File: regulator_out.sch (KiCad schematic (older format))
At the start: 36 parts

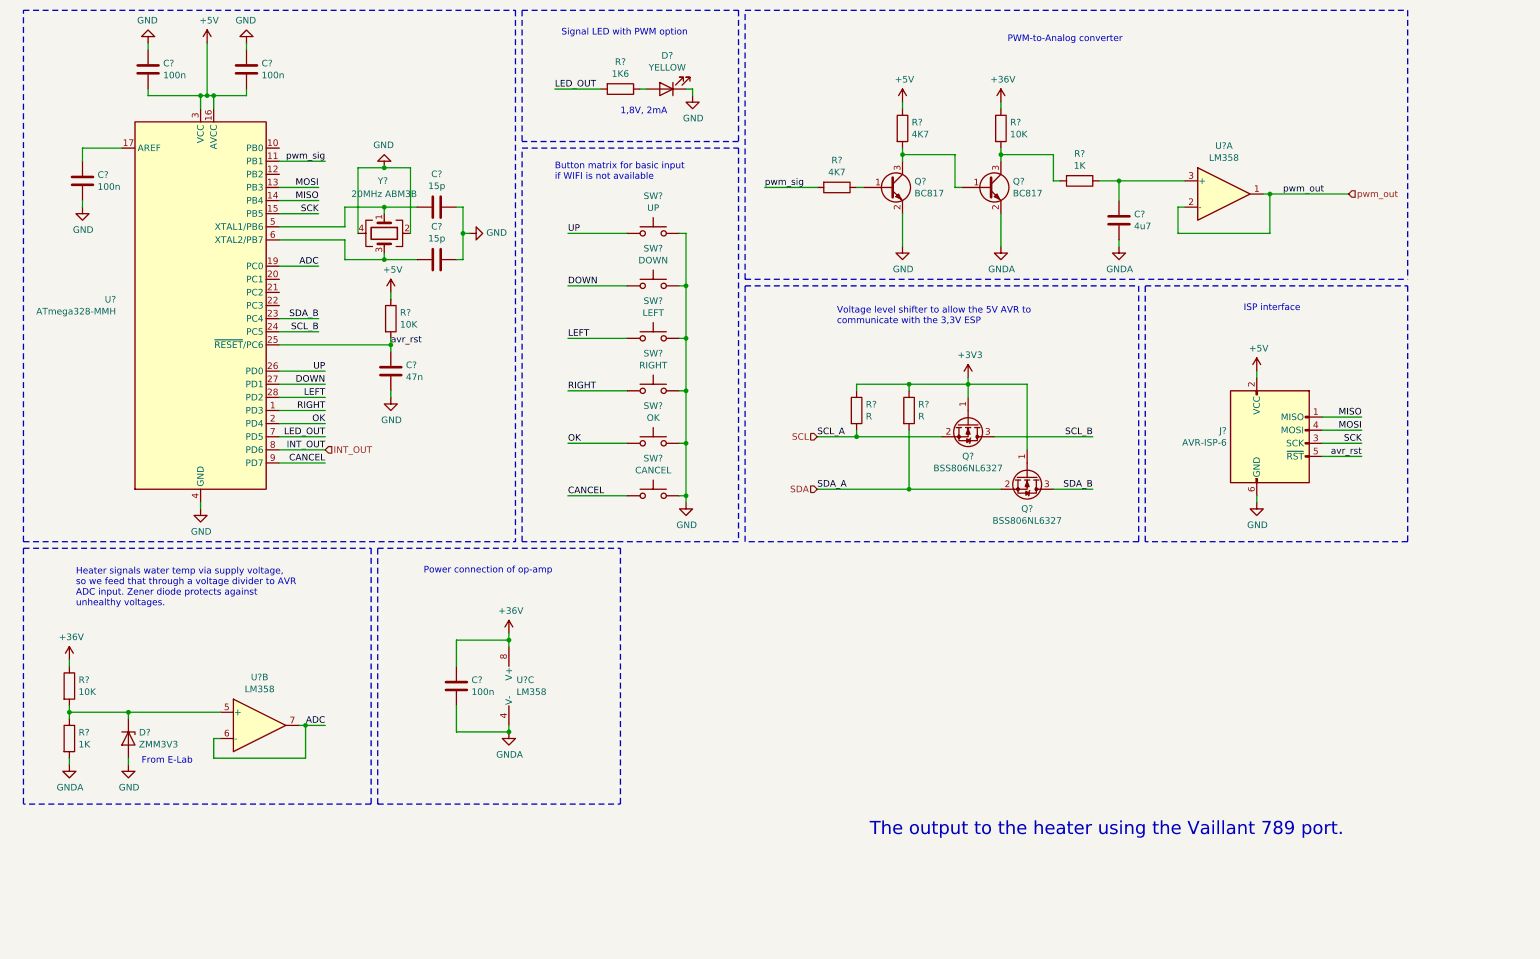
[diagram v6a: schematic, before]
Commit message: Added footprints to most symbols.
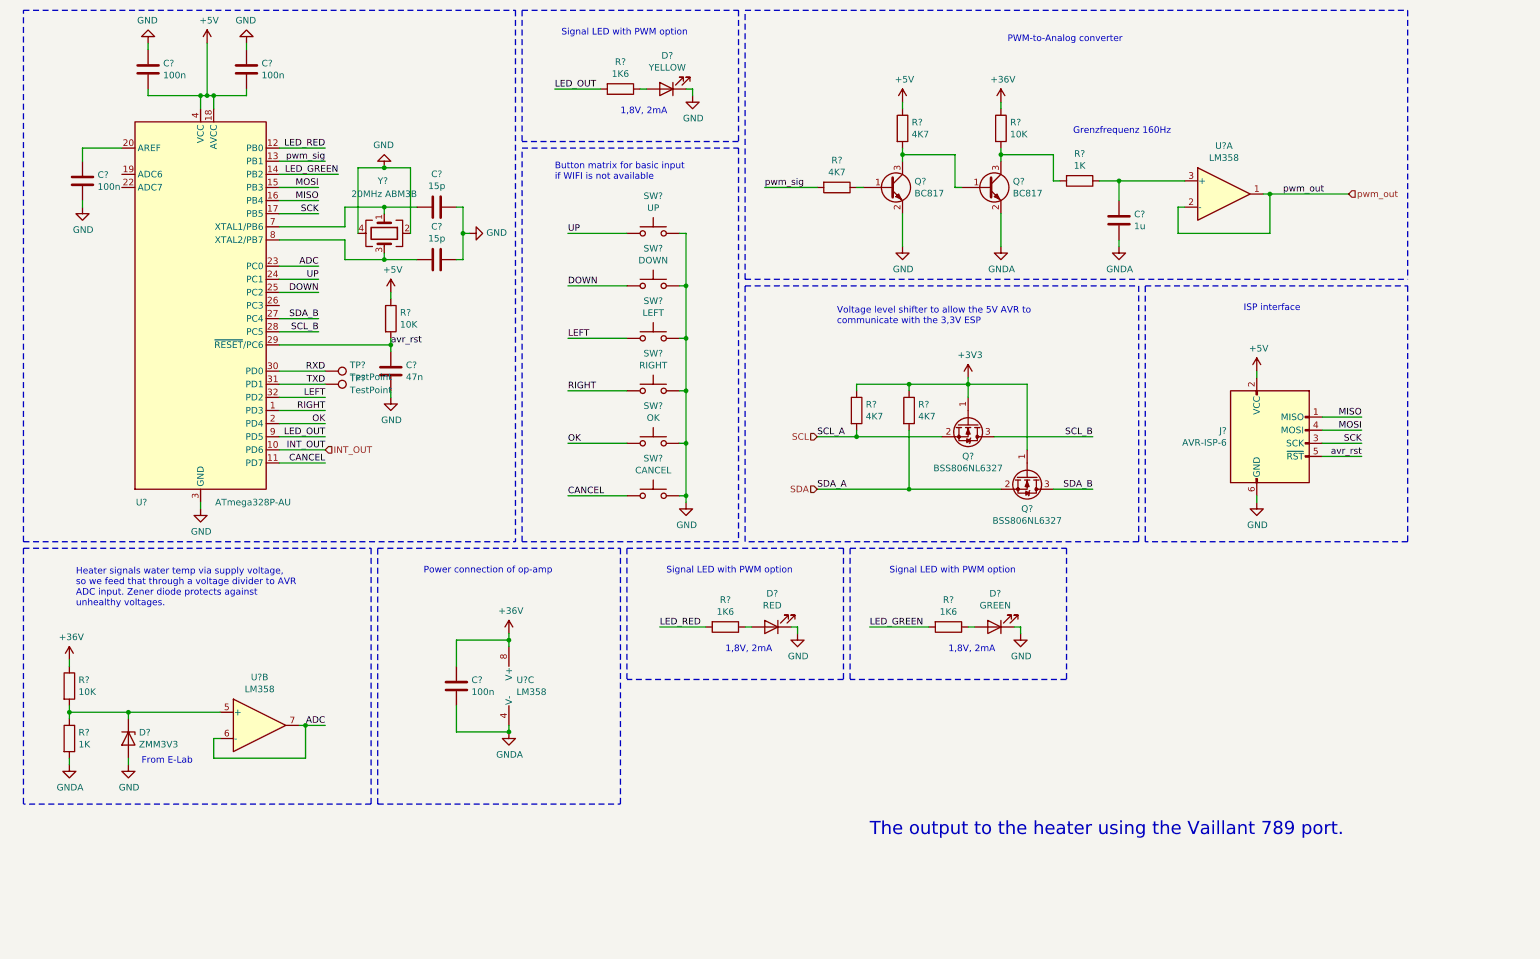
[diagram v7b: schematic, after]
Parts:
- removed U?: ATmega328-MMH, Package_DFN_QFN:QFN-28-1EP_4x4mm_P0.45mm_EP2.4x2.4mm, symbol MCU_Microchip_ATmega:ATmega328-MMH
- added D?: RED, LED_SMD:LED_1210_3225Metric, symbol Device:LED
- added D?: GREEN, LED_SMD:LED_1210_3225Metric, symbol Device:LED
- added R? (x2): 1K6, Resistor_SMD:R_0603_1608Metric, symbol Device:R
- added TP? (x2): TestPoint, symbol Connector:TestPoint
- added U?: ATmega328P-AU, Package_QFP:TQFP-32_7x7mm_P0.8mm, symbol MCU_Microchip_ATmega:ATmega328P-AU
- C?: value 4u7 -> 1u
- D?: footprint (none) -> LED_SMD:LED_1210_3225Metric
- Q? (x4): footprint (none) -> Package_TO_SOT_SMD:SOT-23
- R? (x8): footprint (none) -> Resistor_SMD:R_0603_1608Metric
- R? (x2): value R -> 4K7; footprint (none) -> Resistor_SMD:R_0603_1608Metric
- SW? (x6): footprint (none) -> Button_Switch_SMD:SW_SPST_Panasonic_EVQPL_3PL_5PL_PT_A08
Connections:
- net +5V: now also U?.18 (AVCC), U?.4 (VCC), U?.6 (VCC)
- net ADC: now also U?.23 (PC0)
- net CANCEL: now also U?.11 (PD7)
- net DOWN: now also U?.25 (PC2)
- net GND: now also D?.1 (K), D?.1 (K), U?.21 (GND), U?.3 (GND), U?.5 (GND)
- net INT_OUT: now also U?.10 (PD6)
- net LED_OUT: now also U?.9 (PD5)
- net LEFT: now also U?.32 (PD2)
- net MISO: now also U?.16 (PB4)
- net MOSI: now also U?.15 (PB3)
- net OK: now also U?.2 (PD4)
- net RIGHT: now also U?.1 (PD3)
- net SCK: now also U?.17 (PB5)
- net SCL_B: now also U?.28 (PC5)
- net SDA_B: now also U?.27 (PC4)
- net UP: now also U?.24 (PC1)
- net avr_rst: now also U?.29 (~RESET~/PC6)
- net pwm_sig: now also U?.13 (PB1)
- net at C?.1: now also U?.20 (AREF)
- net at C?.2, Y?.1: now also U?.7 (XTAL1/PB6)
- net at C?.2, Y?.3: now also U?.8 (XTAL2/PB7)
- new net: D?.2 (A), R?.1 (x2)
- new net LED_GREEN: R?.2, U?.14 (PB2)
- new net LED_RED: R?.2, U?.12 (PB0)
- new net RXD: TP?.1, U?.30 (PD0)
- new net TXD: TP?.1, U?.31 (PD1)
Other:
- note added: "Grenzfrequenz 160Hz"

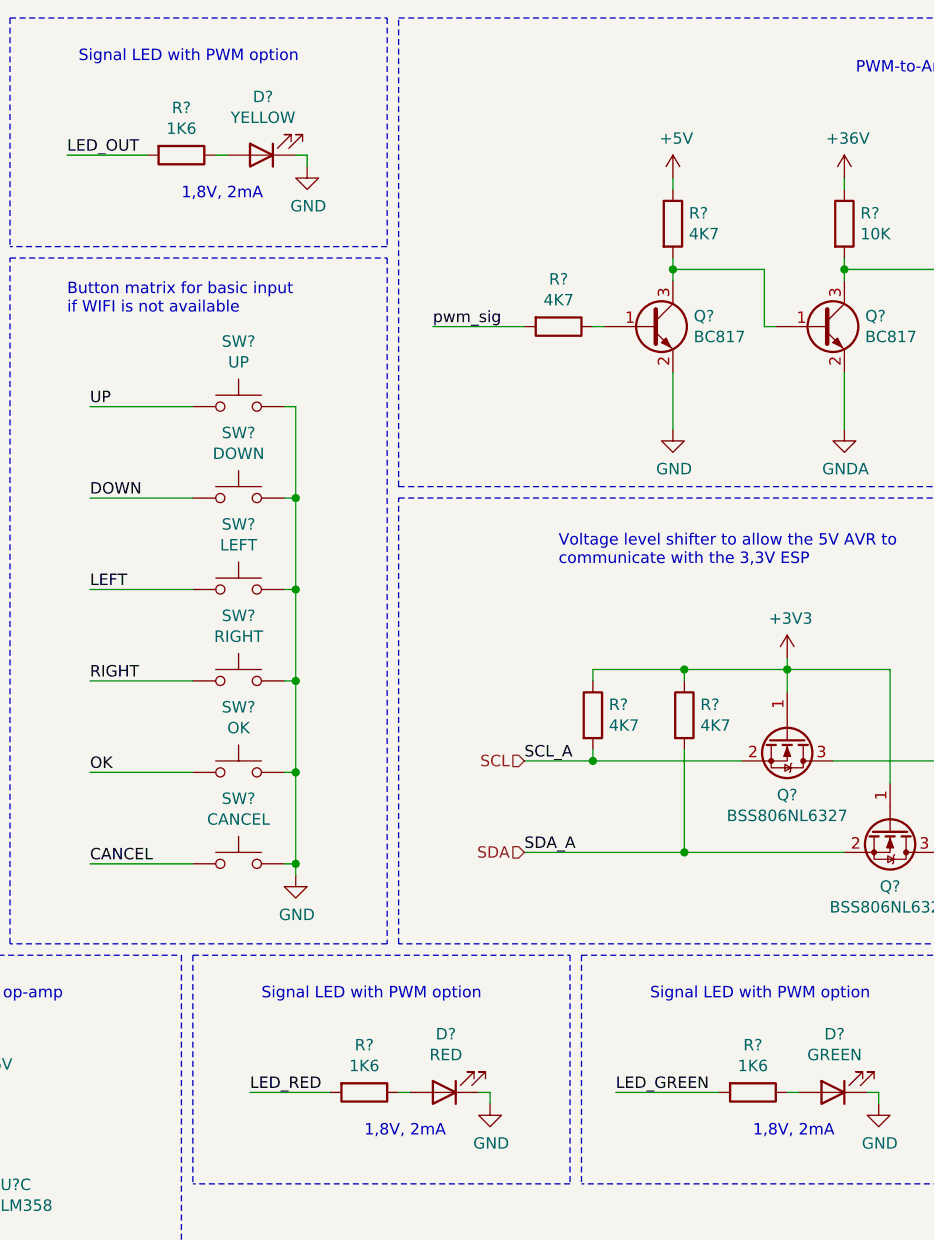
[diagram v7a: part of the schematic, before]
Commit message: Added all footprints except for ones which I have to look up in the E-Lab.
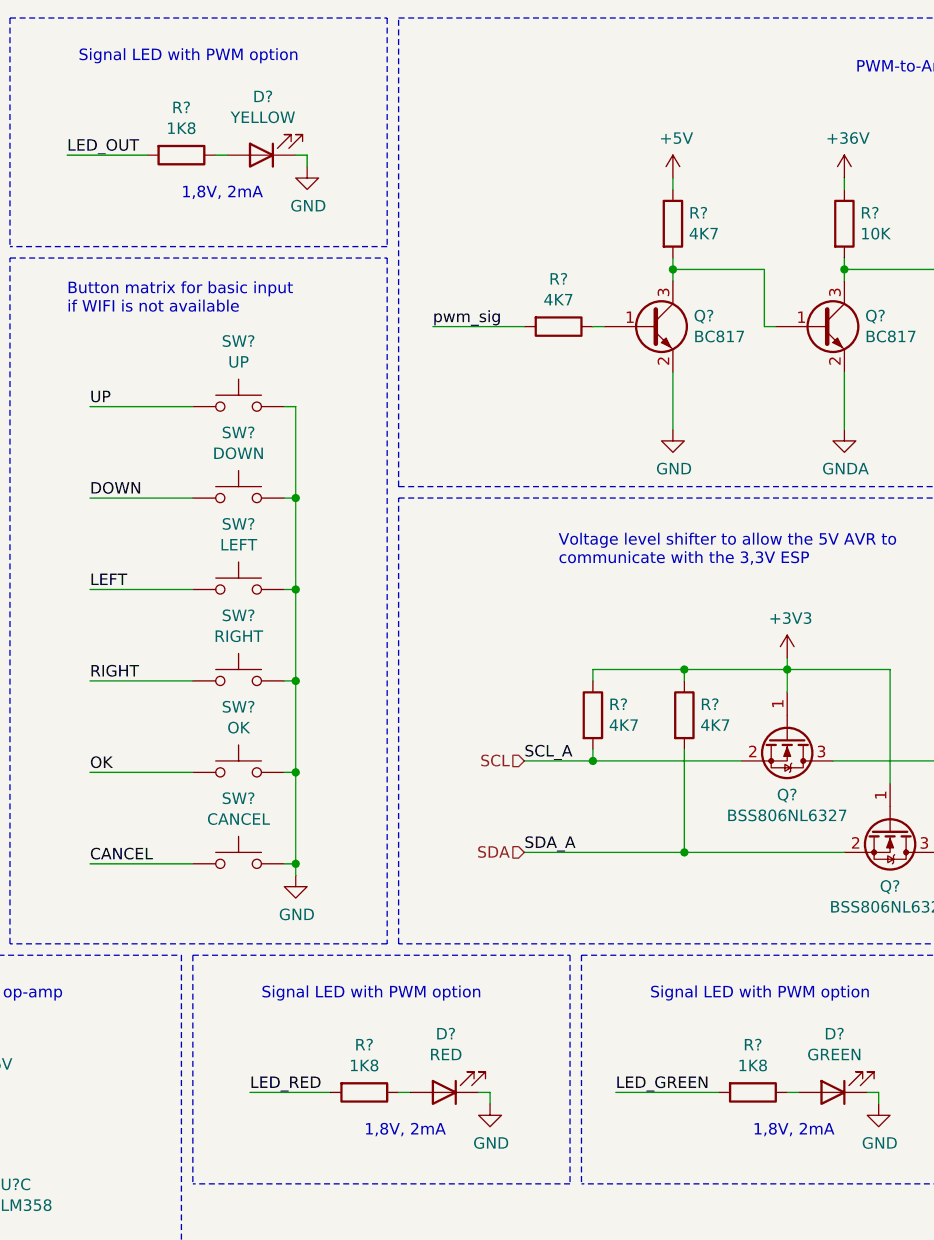
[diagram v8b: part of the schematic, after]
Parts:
- J?: footprint (none) -> Connector_PinHeader_2.54mm:PinHeader_2x03_P2.54mm_Vertical_SMD
- R? (x3): value 1K6 -> 1K8
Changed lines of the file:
@@
 F 0 "J?" H 9771 3996 50  0000 R CNN
 F 1 "AVR-ISP-6" H 9771 3905 50  0000 R CNN
-F 2 "" V 9850 3950 50  0001 C CNN
+F 2 "Connector_PinHeader_2.54mm:PinHeader_2x03_P2.54mm_Vertical_SMD" V 9850 3950 50  0001 C CNN
 F 3 " ~" H 8825 3350 50  0001 C CNN
 	1    10100 3900
@@
 P 5150 1200
 F 0 "R?" V 4943 1200 50  0000 C CNN
-F 1 "1K6" V 5034 1200 50  0000 C CNN
+F 1 "1K8" V 5034 1200 50  0000 C CNN
 F 2 "Resistor_SMD:R_0603_1608Metric" V 5080 1200 50  0001 C CNN
 F 3 "~" H 5150 1200 50  0001 C CNN
@@
 P 5950 5300
 F 0 "R?" V 5743 5300 50  0000 C CNN
-F 1 "1K6" V 5834 5300 50  0000 C CNN
+F 1 "1K8" V 5834 5300 50  0000 C CNN
 F 2 "Resistor_SMD:R_0603_1608Metric" V 5880 5300 50  0001 C CNN
 F 3 "~" H 5950 5300 50  0001 C CNN
@@
 P 7650 5300
 F 0 "R?" V 7443 5300 50  0000 C CNN
-F 1 "1K6" V 7534 5300 50  0000 C CNN
+F 1 "1K8" V 7534 5300 50  0000 C CNN
 F 2 "Resistor_SMD:R_0603_1608Metric" V 7580 5300 50  0001 C CNN
 F 3 "~" H 7650 5300 50  0001 C CNN
